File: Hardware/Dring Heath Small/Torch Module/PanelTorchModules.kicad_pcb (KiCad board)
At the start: 2 copper layers, 137.5 x 130 mm, 172 parts, among them J1 Torch, J10 Module conn, J2 Module3, J4 Limit, J7 Module1, J8 Torch, J9 2.54 pin, K1 G6E, Q1 IRLML2402

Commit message: mounting hole in module board
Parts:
- added REF**: MountingHole_2.7mm, MountingHole:MountingHole_2.7mm, F.Cu at (111.1, 147.0)
- added REF**: MountingHole_2.7mm, MountingHole:MountingHole_2.7mm, F.Cu at (151.1, 147.0)
- added REF**: MountingHole_2.7mm, MountingHole:MountingHole_2.7mm, F.Cu at (191.1, 146.9)
- added REF**: MountingHole_2.7mm, MountingHole:MountingHole_2.7mm, F.Cu at (191.1, 97.4)
- added REF**: MountingHole_2.7mm, MountingHole:MountingHole_2.7mm, F.Cu at (151.1, 97.4)
- added REF**: MountingHole_2.7mm, MountingHole:MountingHole_2.7mm, F.Cu at (111.1, 97.3)

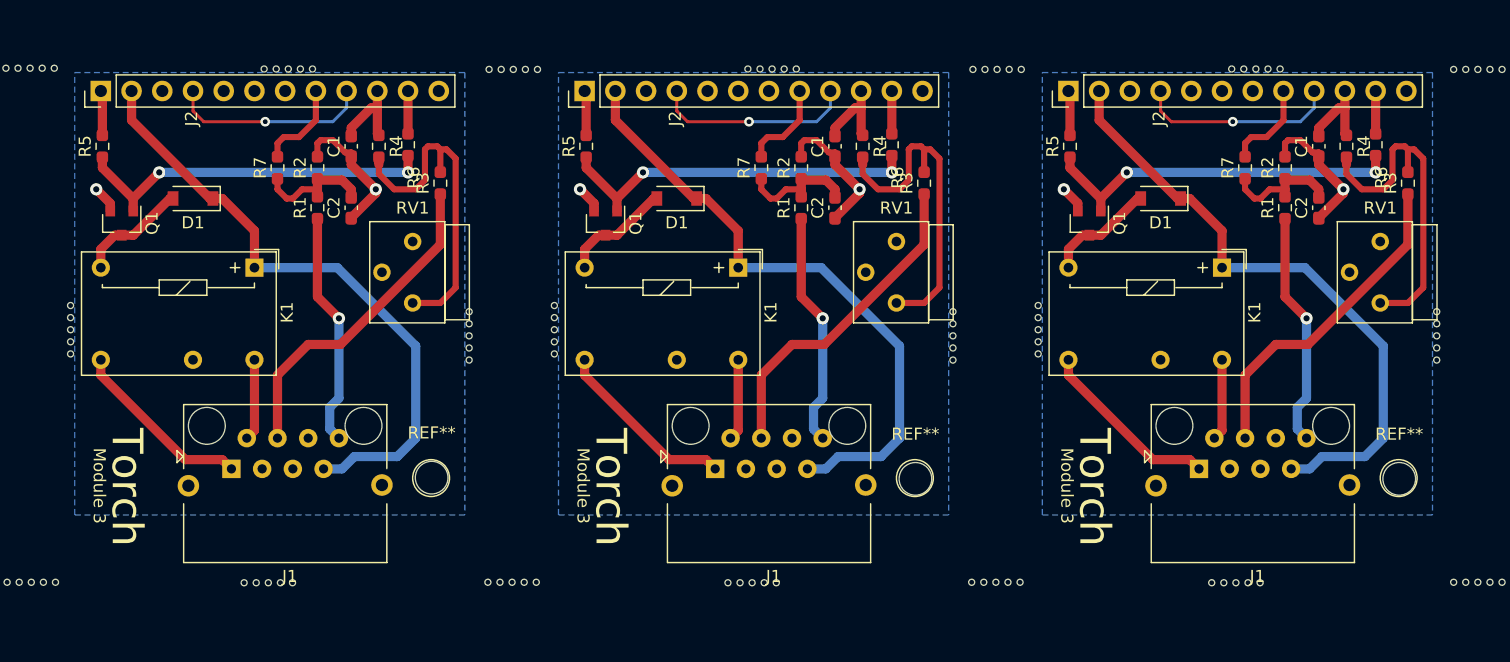
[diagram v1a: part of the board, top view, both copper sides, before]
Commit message: fixed voltage divider for THC
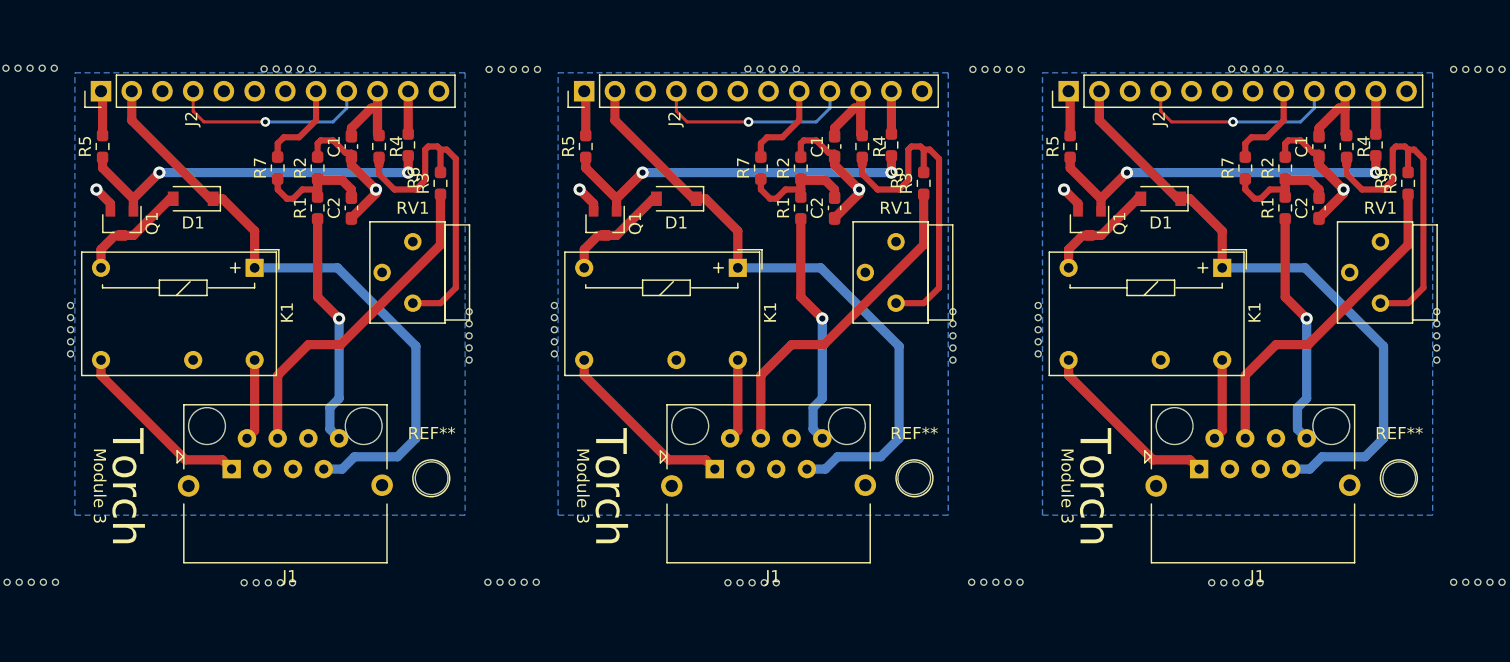
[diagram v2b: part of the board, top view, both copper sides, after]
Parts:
- removed the C1 at (104.5, 69.9)
- removed the C1 at (144.5, 69.9)
- removed the C1 at (184.5, 69.9)
- removed the C2 at (104.5, 75.0)
- removed the C2 at (144.5, 75.0)
- removed the C2 at (184.5, 75.0)
- removed the D1 at (91.4, 74.2)
- removed the D1 at (131.4, 74.2)
- removed the D1 at (171.4, 74.2)
- removed the J1 at (94.5, 95.6)
- removed the J1 at (134.5, 95.6)
- removed the J1 at (174.5, 95.6)
- removed the J2 at (83.7, 65.3)
- removed the J2 at (123.7, 65.3)
- removed the J2 at (163.7, 65.3)
- removed the K1 at (96.4, 79.9)
- removed the K1 at (136.4, 79.9)
- removed the K1 at (176.4, 79.9)
- removed the Q1 at (85.5, 76.3)
- removed the Q1 at (125.5, 76.3)
- removed the Q1 at (165.5, 76.3)
- removed the R1 at (101.7, 75.0)
- removed the R1 at (141.7, 75.0)
- removed the R1 at (181.7, 75.0)
- removed the R2 at (101.7, 71.7)
- removed the R2 at (141.7, 71.7)
- removed the R2 at (181.7, 71.7)
- removed the R3 at (111.8, 73.0)
- removed the R3 at (151.8, 73.0)
- removed the R3 at (191.8, 73.0)
- removed the R4 at (106.7, 69.9)
- removed the R4 at (146.7, 69.9)
- removed the R4 at (186.7, 69.9)
- removed the R5 at (83.9, 69.9)
- removed the R5 at (123.9, 69.9)
- removed the R5 at (163.9, 69.9)
- removed the R6 at (109.1, 69.8)
- removed the R6 at (149.1, 69.8)
- removed the R6 at (189.1, 69.8)
- removed the R7 at (98.4, 71.7)
- removed the R7 at (138.4, 71.7)
- removed the R7 at (178.4, 71.7)
- removed the REF** at (191.1, 97.4)
- removed the REF** at (151.1, 97.4)
- removed the REF** at (111.1, 97.3)
- removed the RV1 at (109.5, 77.8)
- removed the RV1 at (149.5, 77.8)
- removed the RV1 at (189.5, 77.8)
- added C1: 100nf, Capacitor_SMD:C_0603_1608Metric_Pad1.08x0.95mm_HandSolder, F.Cu at (184.5, 69.9)
- added C1: 100nf, Capacitor_SMD:C_0603_1608Metric_Pad1.08x0.95mm_HandSolder, F.Cu at (144.4, 69.9)
- added C1: 100nf, Capacitor_SMD:C_0603_1608Metric_Pad1.08x0.95mm_HandSolder, F.Cu at (104.5, 69.9)
- added C2: 1uf, Capacitor_SMD:C_0603_1608Metric_Pad1.08x0.95mm_HandSolder, F.Cu at (184.5, 75.0)
- added C2: 1uf, Capacitor_SMD:C_0603_1608Metric_Pad1.08x0.95mm_HandSolder, F.Cu at (144.4, 75.0)
- added C2: 1uf, Capacitor_SMD:C_0603_1608Metric_Pad1.08x0.95mm_HandSolder, F.Cu at (104.5, 75.0)
- added D1: D, Diode_SMD:D_SOD-123, F.Cu at (171.4, 74.2)
- added D1: D, Diode_SMD:D_SOD-123, F.Cu at (131.3, 74.2)
- added D1: D, Diode_SMD:D_SOD-123, F.Cu at (91.4, 74.2)
- added J1: Torch, Modules:RJ45_Torb_Vertical, F.Cu at (174.6, 95.6)
- added J1: Torch, Modules:RJ45_Torb_Vertical, F.Cu at (134.5, 95.6)
- added J1: Torch, Modules:RJ45_Torb_Vertical, F.Cu at (94.6, 95.6)
- added J2: Module3, Connector_PinHeader_2.54mm:PinHeader_1x12_P2.54mm_Vertical, F.Cu at (163.8, 65.3)
- added J2: Module3, Connector_PinHeader_2.54mm:PinHeader_1x12_P2.54mm_Vertical, F.Cu at (123.7, 65.3)
- added J2: Module3, Connector_PinHeader_2.54mm:PinHeader_1x12_P2.54mm_Vertical, F.Cu at (83.8, 65.3)
- added K1: G6E, Relay_THT:Relay_SPDT_Omron_G6E, F.Cu at (176.5, 80.0)
- added K1: G6E, Relay_THT:Relay_SPDT_Omron_G6E, F.Cu at (136.4, 80.0)
- added K1: G6E, Relay_THT:Relay_SPDT_Omron_G6E, F.Cu at (96.5, 80.0)
- added Q1: IRLML2402, Package_TO_SOT_SMD:SOT-23, F.Cu at (165.5, 76.3)
- added Q1: IRLML2402, Package_TO_SOT_SMD:SOT-23, F.Cu at (125.4, 76.3)
- added Q1: IRLML2402, Package_TO_SOT_SMD:SOT-23, F.Cu at (85.5, 76.3)
- added R1: 3.3K, Resistor_SMD:R_0603_1608Metric_Pad0.98x0.95mm_HandSolder, F.Cu at (181.7, 75.0)
- added R1: 3.3K, Resistor_SMD:R_0603_1608Metric_Pad0.98x0.95mm_HandSolder, F.Cu at (141.6, 75.0)
- added R1: 3.3K, Resistor_SMD:R_0603_1608Metric_Pad0.98x0.95mm_HandSolder, F.Cu at (101.7, 75.0)
- added R2: 1k, Resistor_SMD:R_0603_1608Metric_Pad0.98x0.95mm_HandSolder, F.Cu at (181.7, 71.7)
- added R2: 1k, Resistor_SMD:R_0603_1608Metric_Pad0.98x0.95mm_HandSolder, F.Cu at (141.6, 71.7)
- added R2: 1k, Resistor_SMD:R_0603_1608Metric_Pad0.98x0.95mm_HandSolder, F.Cu at (101.7, 71.7)
- added R3: 3.3K, Resistor_SMD:R_0603_1608Metric_Pad0.98x0.95mm_HandSolder, F.Cu at (191.8, 73.0)
- added R3: 3.3K, Resistor_SMD:R_0603_1608Metric_Pad0.98x0.95mm_HandSolder, F.Cu at (151.8, 73.0)
- added R3: 3.3K, Resistor_SMD:R_0603_1608Metric_Pad0.98x0.95mm_HandSolder, F.Cu at (111.8, 73.0)
- added R4: 10k, Resistor_SMD:R_0603_1608Metric_Pad0.98x0.95mm_HandSolder, F.Cu at (186.8, 69.9)
- added R4: 10k, Resistor_SMD:R_0603_1608Metric_Pad0.98x0.95mm_HandSolder, F.Cu at (146.7, 69.9)
- added R4: 10k, Resistor_SMD:R_0603_1608Metric_Pad0.98x0.95mm_HandSolder, F.Cu at (106.8, 69.9)
- added R5: 10k, Resistor_SMD:R_0603_1608Metric_Pad0.98x0.95mm_HandSolder, F.Cu at (163.9, 69.9)
- added R5: 10k, Resistor_SMD:R_0603_1608Metric_Pad0.98x0.95mm_HandSolder, F.Cu at (123.8, 69.9)
- added R5: 10k, Resistor_SMD:R_0603_1608Metric_Pad0.98x0.95mm_HandSolder, F.Cu at (83.9, 69.9)
- added R6: 200, Resistor_SMD:R_0603_1608Metric_Pad0.98x0.95mm_HandSolder, F.Cu at (189.2, 69.8)
- added R6: 200, Resistor_SMD:R_0603_1608Metric_Pad0.98x0.95mm_HandSolder, F.Cu at (149.1, 69.8)
- added R6: 200, Resistor_SMD:R_0603_1608Metric_Pad0.98x0.95mm_HandSolder, F.Cu at (109.2, 69.8)
- added R7: 200, Resistor_SMD:R_0603_1608Metric_Pad0.98x0.95mm_HandSolder, F.Cu at (178.4, 71.7)
- added R7: 200, Resistor_SMD:R_0603_1608Metric_Pad0.98x0.95mm_HandSolder, F.Cu at (138.3, 71.7)
- added R7: 200, Resistor_SMD:R_0603_1608Metric_Pad0.98x0.95mm_HandSolder, F.Cu at (98.4, 71.7)
- added REF**: MountingHole_2.7mm, MountingHole:MountingHole_2.7mm, F.Cu at (111.1, 97.3)
- added REF**: MountingHole_2.7mm, MountingHole:MountingHole_2.7mm, F.Cu at (151.0, 97.3)
- added REF**: MountingHole_2.7mm, MountingHole:MountingHole_2.7mm, F.Cu at (191.1, 97.3)
- added RV1: 2K, Potentiometer_THT:Potentiometer_Bourns_3339S_Horizontal, F.Cu at (189.5, 77.8)
- added RV1: 2K, Potentiometer_THT:Potentiometer_Bourns_3339S_Horizontal, F.Cu at (149.5, 77.8)
- added RV1: 2K, Potentiometer_THT:Potentiometer_Bourns_3339S_Horizontal, F.Cu at (109.5, 77.8)

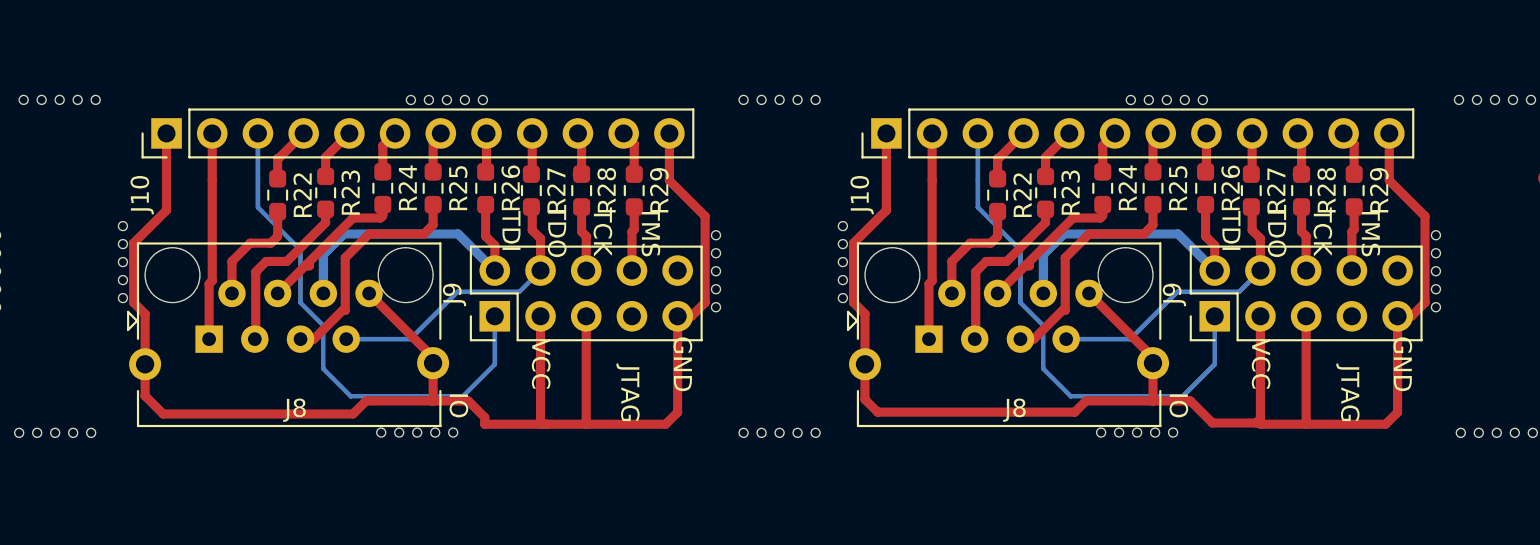
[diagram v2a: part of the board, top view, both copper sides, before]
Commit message: added A/D to panel
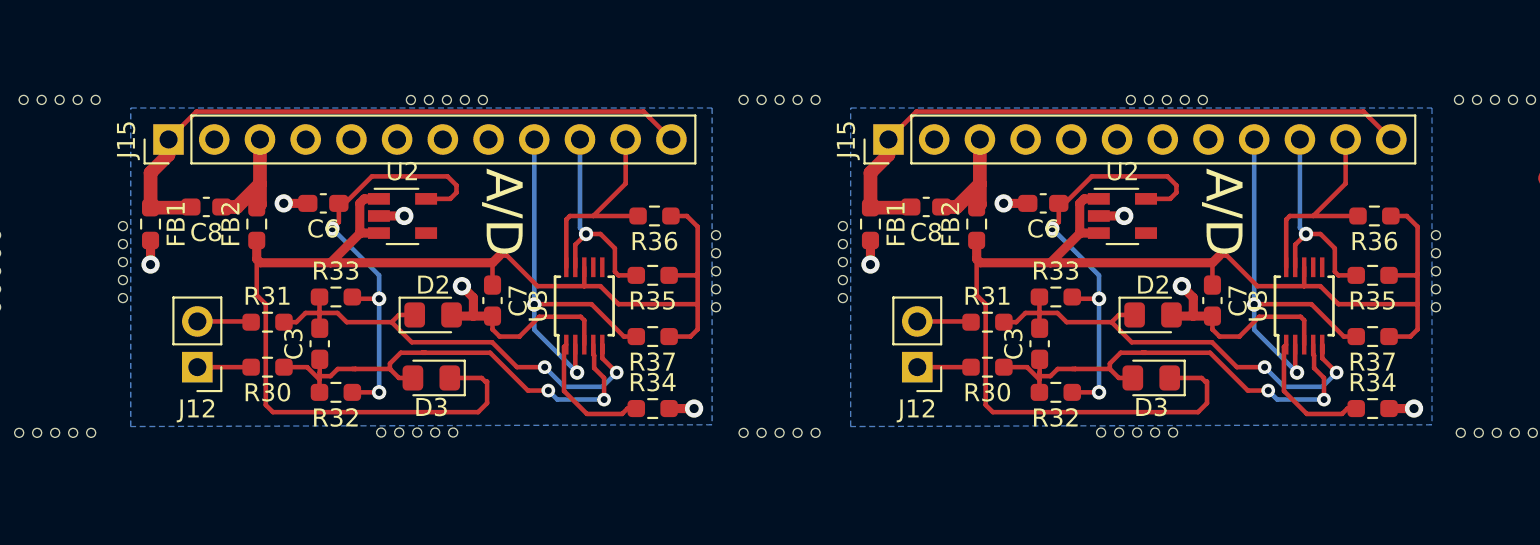
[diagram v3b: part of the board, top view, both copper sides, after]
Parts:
- removed the J10 at (123.7, 39.8)
- removed the J10 at (163.7, 39.8)
- removed the J8 at (126.1, 50.2)
- removed the J8 at (166.1, 50.2)
- removed the J9 at (141.9, 50.0)
- removed the J9 at (181.9, 50.0)
- removed the R22 at (129.9, 43.2)
- removed the R22 at (169.9, 43.2)
- removed the R23 at (132.5, 43.1)
- removed the R23 at (172.5, 43.1)
- removed the R24 at (135.7, 42.9)
- removed the R24 at (175.7, 42.9)
- removed the R25 at (138.5, 42.9)
- removed the R25 at (178.5, 42.9)
- removed the R26 at (141.4, 42.9)
- removed the R26 at (181.4, 42.9)
- removed the R27 at (144.0, 43.0)
- removed the R27 at (184.0, 43.0)
- removed the R28 at (146.8, 43.0)
- removed the R28 at (186.8, 43.0)
- removed the R29 at (149.7, 43.0)
- removed the R29 at (189.7, 43.0)
- added C3: 100nf, Capacitor_SMD:C_0603_1608Metric_Pad1.08x0.95mm_HandSolder, F.Cu at (172.2, 51.5)
- added C3: 100nf, Capacitor_SMD:C_0603_1608Metric_Pad1.08x0.95mm_HandSolder, F.Cu at (132.2, 51.5)
- added C6: 1uf, Capacitor_SMD:C_0603_1608Metric_Pad1.08x0.95mm_HandSolder, F.Cu at (172.4, 43.7)
- added C6: 1uf, Capacitor_SMD:C_0603_1608Metric_Pad1.08x0.95mm_HandSolder, F.Cu at (132.4, 43.7)
- added C7: 100nf, Capacitor_SMD:C_0603_1608Metric_Pad1.08x0.95mm_HandSolder, F.Cu at (181.8, 49.1)
- added C7: 100nf, Capacitor_SMD:C_0603_1608Metric_Pad1.08x0.95mm_HandSolder, F.Cu at (141.8, 49.1)
- added C8: 1uf, Capacitor_SMD:C_0603_1608Metric_Pad1.08x0.95mm_HandSolder, F.Cu at (165.9, 43.9)
- added C8: 1uf, Capacitor_SMD:C_0603_1608Metric_Pad1.08x0.95mm_HandSolder, F.Cu at (125.9, 43.9)
- added D2: D_Schottky_Small, Diode_SMD:D_0805_2012Metric_Pad1.15x1.40mm_HandSolder, F.Cu at (178.5, 49.9)
- added D2: D_Schottky_Small, Diode_SMD:D_0805_2012Metric_Pad1.15x1.40mm_HandSolder, F.Cu at (138.5, 49.9)
- added D3: D_Schottky_Small, Diode_SMD:D_0805_2012Metric_Pad1.15x1.40mm_HandSolder, F.Cu at (178.4, 53.4)
- added D3: D_Schottky_Small, Diode_SMD:D_0805_2012Metric_Pad1.15x1.40mm_HandSolder, F.Cu at (138.4, 53.4)
- added FB1: BLM18HE152SN1D, Resistor_SMD:R_0603_1608Metric_Pad0.98x0.95mm_HandSolder, F.Cu at (162.8, 44.9)
- added FB1: BLM18HE152SN1D, Resistor_SMD:R_0603_1608Metric_Pad0.98x0.95mm_HandSolder, F.Cu at (122.8, 44.9)
- added FB2: ~, Resistor_SMD:R_0603_1608Metric_Pad0.98x0.95mm_HandSolder, F.Cu at (168.7, 44.9)
- added FB2: ~, Resistor_SMD:R_0603_1608Metric_Pad0.98x0.95mm_HandSolder, F.Cu at (128.7, 44.9)
- added J12: Conn_01x02_Male, Connector_PinHeader_2.54mm:PinHeader_1x02_P2.54mm_Vertical, F.Cu at (165.4, 52.8)
- added J12: Conn_01x02_Male, Connector_PinHeader_2.54mm:PinHeader_1x02_P2.54mm_Vertical, F.Cu at (125.4, 52.8)
- added J15: Module conn, Connector_PinHeader_2.54mm:PinHeader_1x12_P2.54mm_Vertical, F.Cu at (163.8, 40.1)
- added J15: Module conn, Connector_PinHeader_2.54mm:PinHeader_1x12_P2.54mm_Vertical, F.Cu at (123.8, 40.1)
- added R30: 1k, Resistor_SMD:R_0603_1608Metric_Pad0.98x0.95mm_HandSolder, F.Cu at (169.3, 52.8)
- added R30: 1k, Resistor_SMD:R_0603_1608Metric_Pad0.98x0.95mm_HandSolder, F.Cu at (129.3, 52.8)
- added R31: 1k, Resistor_SMD:R_0603_1608Metric_Pad0.98x0.95mm_HandSolder, F.Cu at (169.3, 50.3)
- added R31: 1k, Resistor_SMD:R_0603_1608Metric_Pad0.98x0.95mm_HandSolder, F.Cu at (129.3, 50.3)
- added R32: 1k, Resistor_SMD:R_0603_1608Metric_Pad0.98x0.95mm_HandSolder, F.Cu at (173.1, 54.2)
- added R32: 1k, Resistor_SMD:R_0603_1608Metric_Pad0.98x0.95mm_HandSolder, F.Cu at (133.1, 54.2)
- added R33: 1k, Resistor_SMD:R_0603_1608Metric_Pad0.98x0.95mm_HandSolder, F.Cu at (173.1, 48.9)
- added R33: 1k, Resistor_SMD:R_0603_1608Metric_Pad0.98x0.95mm_HandSolder, F.Cu at (133.1, 48.9)
- added R34: 2.4K, Resistor_SMD:R_0603_1608Metric_Pad0.98x0.95mm_HandSolder, F.Cu at (190.7, 55.1)
- added R34: 2.4K, Resistor_SMD:R_0603_1608Metric_Pad0.98x0.95mm_HandSolder, F.Cu at (150.7, 55.1)
- added R35: 2.4K, Resistor_SMD:R_0603_1608Metric_Pad0.98x0.95mm_HandSolder, F.Cu at (190.7, 47.7)
- added R35: 2.4K, Resistor_SMD:R_0603_1608Metric_Pad0.98x0.95mm_HandSolder, F.Cu at (150.7, 47.7)
- added R36: 2.4K, Resistor_SMD:R_0603_1608Metric_Pad0.98x0.95mm_HandSolder, F.Cu at (190.8, 44.4)
- added R36: 2.4K, Resistor_SMD:R_0603_1608Metric_Pad0.98x0.95mm_HandSolder, F.Cu at (150.8, 44.4)
- added R37: 2.4K, Resistor_SMD:R_0603_1608Metric_Pad0.98x0.95mm_HandSolder, F.Cu at (190.7, 51.1)
- added R37: 2.4K, Resistor_SMD:R_0603_1608Metric_Pad0.98x0.95mm_HandSolder, F.Cu at (150.7, 51.1)
- added U2: NCV8114ASN150T1G, Package_TO_SOT_SMD:TSOT-23-5, F.Cu at (176.8, 44.4)
- added U2: NCV8114ASN150T1G, Package_TO_SOT_SMD:TSOT-23-5, F.Cu at (136.8, 44.4)
- added U3: ADS1115IDGS, Package_SO:TSSOP-10_3x3mm_P0.5mm, F.Cu at (186.9, 49.4)
- added U3: ADS1115IDGS, Package_SO:TSSOP-10_3x3mm_P0.5mm, F.Cu at (146.9, 49.4)
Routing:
- net Net-(J10-Pad1): track 251.7 -> 83.8 mm
- net Net-(C7-Pad1): track 0.00 -> 141.1 mm
- net Net-(C8-Pad2): track 0.00 -> 71.4 mm
- net Net-(J10-Pad3): track 84.4 -> 28.1 mm
- net Net-(C3-Pad1): track 0.00 -> 53.4 mm, vias 0 -> 4
- net Net-(C3-Pad2): track 0.00 -> 52.5 mm, vias 0 -> 4
- net Net-(C6-Pad1): track 0.00 -> 48.7 mm, vias 0 -> 6
- net Net-(J15-Pad9): track 0.00 -> 43.9 mm, vias 0 -> 4
- net Net-(C6-Pad2): track 0.00 -> 35.2 mm, vias 0 -> 10
- net Net-(J8-Pad6): track 50.8 -> 16.9 mm
- net Net-(J8-Pad7): track 48.5 -> 16.2 mm
- net Net-(J8-Pad5): track 38.5 -> 12.8 mm
- net Net-(J15-Pad10): track 0.00 -> 24.0 mm, vias 0 -> 2
- net Net-(J15-Pad11): track 0.00 -> 23.4 mm
- net Net-(J10-Pad2): track 34.5 -> 11.5 mm
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- added copper zone on B.Cu, net Net-(C6-Pad2)
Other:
- board text added: "A/D"
